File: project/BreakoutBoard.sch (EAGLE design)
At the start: 2 parts, among them J1 XF2L-2435-1, X1 LCD

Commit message: Layout complete
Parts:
- added B1: RESET, alps:SKSCLDE010
- added B2: BOOT, alps:SKSCLDE010
- added C1: 22pF/50V, SparkFun-Capacitors:22PF-0402T-16V-10%
- added C105: 2.2uF/16V, rcl:C-EUC0603
- added C106: 4.7uF/16V, rcl:C-EUC0603
- added C107: 22pF/50V, rcl:C-EUC0402
- added C17: 10uF/16V, rcl:C-EUC0603
- added C18: 0.1uF/10V, rcl:C-EUC0402
- added C19: 1uF/16V, rcl:C-EUC0402
- added C2, C5: 10uF/16V, SparkFun-Capacitors:10UF-0603-6.3V-20%
- added C3, C4: 0.1uF/10V, SparkFun-Capacitors:0.1UF-0402-10V-10%-X7R
- added C86: (no value), rcl:C-EUC0402
- added CN2: (no value), adafruit:JST_2PIN-SMT
- added D1, D15: (no value), diode:DIODE-SOD123
- added D10, D8, D9: LESD5D5.0CT1G, discrete:LESD5D5.0CT1G
- added D11, D12, D2: LESD8D3.3CAT5G, discrete:LESD8D3.3CAT5G
- added D19: (no value), adafruit:DIODESOD-523
- added D3: (no value), led:LEDCHIPLED_1206
- added J2: I2C2, SparkFun-Connectors:QWIIC_CONNECTOR
- added J3: LCD, ER-CON0.4-24P:ER-CON0.4-24
- added L1: 2.2μH, SparkFun-Coils:2.2μH-4X4-2.2μH-3A-45MOHM
- added L6: 10uH_0.8A, discrete:SRN3010TA
- added R1, R13: 10K, rcl:R-US_R0402
- added R111, R112: 0, rcl:R-US_R0201
- added R12, R123: 0, rcl:R-US_R0603
- added R126: 6.6, rcl:R-US_R0402
- added R127: 10, rcl:R-US_R0402
- added R2: 680K, rcl:R-US_R0402
- added R3: 150K, rcl:R-US_R0402
- added R74: 51, rcl:R-US_R0201
- added TP1, TP2: TEST-POINT3, SparkFun-Connectors:TEST-POINT3
- added U1: SY8088, discrete:SY8088
- added U15: BD60A60NUX, discrete:BD60A60NUX
- added U4: ESP32-S3-WROOM-1, espressif:ESP32-S3-WROOM-1
- J1: value XF2L-2435-1 -> I2C1; device con-omron:XF2L-2435-1 -> SparkFun-Connectors:QWIIC_CONNECTOR
- X1: value LCD -> (none); device ER-CON0.4-24P:ER-CON0.4-24 -> Adafruit ItsyBitsy nRF52840 Express:MICROBUILDER_USBMICRO_20329
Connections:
- removed net N$10: J1-10.MS, X1-10.1
- removed net N$11: J1-11.MS, X1-11.1
- removed net N$12: J1-12.MS, X1-12.1
- removed net N$13: J1-13.MS, X1-13.1
- removed net N$14: J1-14.MS, X1-14.1
- removed net N$15: J1-15.MS, X1-15.1
- removed net N$16: J1-16.MS, X1-16.1
- removed net N$17: J1-17.MS, X1-17.1
- removed net N$18: J1-18.MS, X1-18.1
- removed net N$19: J1-19.MS, X1-19.1
- removed net N$20: J1-20.MS, X1-20.1
- removed net N$21: J1-21.MS, X1-21.1
- removed net N$22: J1-22.MS, X1-22.1
- removed net N$23: J1-23.MS, X1-23.1
- removed net N$24: J1-24.MS, X1-24.1
- removed net N$3: J1-3.MS, X1-3.1
- removed net N$5: J1-5.MS, X1-5.1
- new net ESP_3V3: C17.1, C18.1, D2.C, R12.2, R13.1, U4.3V3
- new net GND: B1.1, B2.1, C105.2, C106.2, C107.2, C17.2, C18.2, C19.2, C2.2, C3.2, C4.2, C5.2, C86.2, CN2.1, D10.A, D11.A, D12.A, D2.A, D8.A, D9.A, J1.1, J2.1, J3-15.1, J3-16.1, J3-3.1, J3-4.1, R123.1, R126.1, R3.1, R74.1, TP2.1, U1.GND, U15.GND, U4.EPAD, U4.GND, U4.GND1
- new net GPIO0: B2.4, D12.C, U4.IO0
- new net GPIO18: J1.4, U4.IO18
- new net GPIO19: R111.2, U4.IO19
- new net GPIO20: R112.2, U4.IO20
- new net GPIO3: J3-21.1, U4.IO3
- new net GPIO4: J3-5.1, U4.IO4
- new net GPIO40: J2.4, J3-20.1, U4.IO40
- new net GPIO41: J2.3, J3-19.1, U4.IO41
- new net GPIO45: R127.1, U4.IO45
- new net GPIO48: J3-10.1, J3-18.1, U15.EN, U4.IO48
- new net GPIO5: J3-9.1, U4.IO5
- new net GPIO6: J3-8.1, U4.IO6
- new net GPIO7: J3-6.1, U4.IO7
- new net GPIO8: J1.3, U4.IO8
- new net LED_A: C105.1, D19.C, J3-23.1, J3-24.1, U15.VOUT
- new net LED_DIM: C107.1, R127.2, U15.PWM
- new net LED_K: J3-1.1, J3-2.1, U15.FB
- new net MCU_RST: B1.4, C19.1, D11.C, R13.2, U4.EN
- new net MCU_VDD: C1.1, C4.1, C5.1, C86.1, D3.A, J1.2, J2.2, J3-11.1, J3-12.1, J3-13.1, J3-14.1, J3-17.1, L1.2, R12.1, R2.2, TP1.1
- new net USB_5V: C106.1, C2.1, C3.1, D1.C, D15.C, L6.1, R1.1, U1.IN, U15.VIN
- new net USB_DN: D9.C, R111.1, X1.D-
- new net USB_DP: D10.C, R112.1, X1.D+
- new net USB_G: R123.2, X1.GND
- new net USB_VBUS: D1.A, D8.C, X1.VBUS
- net N$1: now also D19.A, L6.2, U15.SW; no longer J1-1.MSV, X1-1.1
- net N$2: now also D3.C, R74.2; no longer J1-2.MS, X1-2.1
- net N$4: now also CN2.2, D15.A; no longer J1-4.MS, X1-4.1
- net N$6: now also R1.2, U1.EN; no longer J1-6.MS, X1-6.1
- net N$7: now also L1.1, U1.LX; no longer J1-7.MS, X1-7.1
- net N$8: now also C1.2, R2.1, R3.2, U1.FB; no longer J1-8.MS, X1-8.1
- net N$9: now also R126.2, U15.ISET; no longer J1-9.MS, X1-9.1

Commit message: Layout optimization
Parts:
- removed C107: 22pF/50V, rcl:C-EUC0402
- removed CN2: (no value), adafruit:JST_2PIN-SMT
- removed R127: 10, rcl:R-US_R0402
- removed TP2: TEST-POINT3, SparkFun-Connectors:TEST-POINT3
- removed X1: (no value), Adafruit ItsyBitsy nRF52840 Express:MICROBUILDER_USBMICRO_20329
- added C97: 0.1uF/6.3V, rcl:C-USC0402
- added C98: 4.7uF/6.3V, rcl:C-USC0402
- added J4: I2C1, SparkFun-Connectors:QWIIC_CONNECTOR
- added J5: I2C2, SparkFun-Connectors:QWIIC_CONNECTOR
- added U$1, U$2, U$4, U$5: FIDUCIAL, adafruit:FIDUCIAL
- B1, B2: LCSC (none) -> C115362
- C1: device SparkFun-Capacitors:22PF-0402T-16V-10% -> rcl:C-USC0402; LCSC (none) -> C106203
- C105: device rcl:C-EUC0603 -> rcl:C-USC0603; LCSC (none) -> C106853
- C106: device rcl:C-EUC0603 -> rcl:C-USC0603; LCSC (none) -> C277476
- C17: device rcl:C-EUC0603 -> rcl:C-USC0603; LCSC (none) -> C86275
- C18: device rcl:C-EUC0402 -> rcl:C-USC0402; LCSC (none) -> C161163
- C19: device rcl:C-EUC0402 -> rcl:C-USC0402; LCSC (none) -> C77007
- C2: device SparkFun-Capacitors:10UF-0603-6.3V-20% -> rcl:C-USC0603; LCSC (none) -> C86275
- C3: device SparkFun-Capacitors:0.1UF-0402-10V-10%-X7R -> rcl:C-USC0603; LCSC (none) -> C161163
- C4: device SparkFun-Capacitors:0.1UF-0402-10V-10%-X7R -> rcl:C-USC0402; LCSC (none) -> C161163
- C5: device SparkFun-Capacitors:10UF-0603-6.3V-20% -> rcl:C-USC0402; LCSC (none) -> C86275
- C86: value (none) -> 0.1uF/6.3V; device rcl:C-EUC0402 -> rcl:C-USC0402; LCSC (none) -> C541406
- D1, D15: LCSC (none) -> C511872
- D10, D8, D9: LCSC (none) -> C383211
- D11, D12, D2: LCSC (none) -> C172409
- D19: LCSC (none) -> C253516
- D3: LCSC (none) -> C375534
- J1: value I2C1 -> (none); device SparkFun-Connectors:QWIIC_CONNECTOR -> Adafruit ItsyBitsy nRF52840 Express:MICROBUILDER_USBMICRO_20329; LCSC (none) -> C40946
- J2: value I2C2 -> (none); device SparkFun-Connectors:QWIIC_CONNECTOR -> adafruit:JST_2PIN-SMT; LCSC (none) -> C64658
- L1: LCSC (none) -> C370436
- L6: LCSC (none) -> C518881
- R1, R13: LCSC (none) -> C60490
- R111, R112: LCSC (none) -> C106227
- R12, R123: LCSC (none) -> C100044
- R126: value 6.6 -> 20K; LCSC (none) -> C326980
- R2: LCSC (none) -> C163456
- R3: LCSC (none) -> C93947
- R74: LCSC (none) -> C163499
- TP1: value TEST-POINT3 -> TPTP06R; device SparkFun-Connectors:TEST-POINT3 -> testpad:TPTP06R
- U1: LCSC (none) -> C79313
- U15: LCSC (none) -> C2678724
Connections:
- removed net LED_DIM: C107.1, R127.2, U15.PWM
- net GND: now also B1.2, B2.2, C97.2, C98.2, J4.1, J5.1; no longer C107.2, CN2.1, J1.1, TP2.1
- net GPIO0: now also B2.3
- net GPIO18: now also J4.4; no longer J1.4
- net GPIO40: now also J5.4; no longer J2.4
- net GPIO41: now also J5.3; no longer J2.3
- net GPIO45: now also U15.PWM; no longer R127.1
- net GPIO8: now also J4.3; no longer J1.3
- net LED_K: now also TP1.TP
- net MCU_RST: now also B1.3
- net MCU_VDD: now also C97.1, C98.1, J4.2, J5.2, U15.VIN; no longer J1.2, J2.2, TP1.1
- net N$4: now also J2.2; no longer CN2.2
- net USB_5V: no longer U15.VIN
- net USB_DN: now also J1.D-; no longer X1.D-
- net USB_DP: now also J1.D+; no longer X1.D+
- net USB_G: now also J1.GND; no longer X1.GND
- net USB_VBUS: now also J1.VBUS; no longer X1.VBUS
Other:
- moved on the sheet: B1, B2, C1, C105, C106, C17, C18, C19, C2, C3, C4, C5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

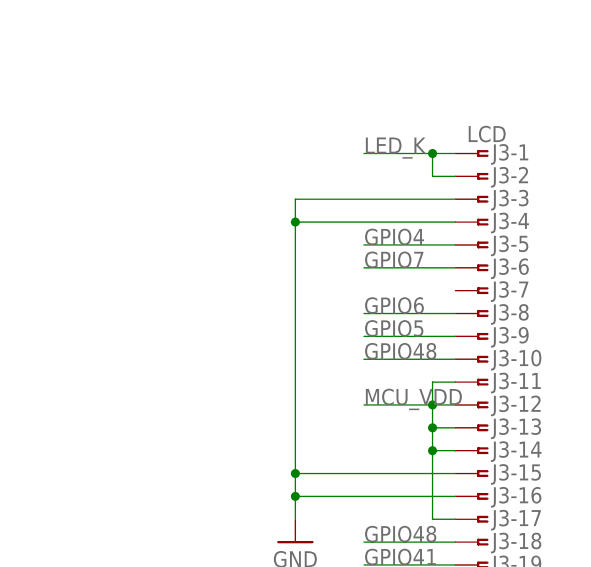
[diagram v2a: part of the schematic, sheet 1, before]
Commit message: Display pinout fix
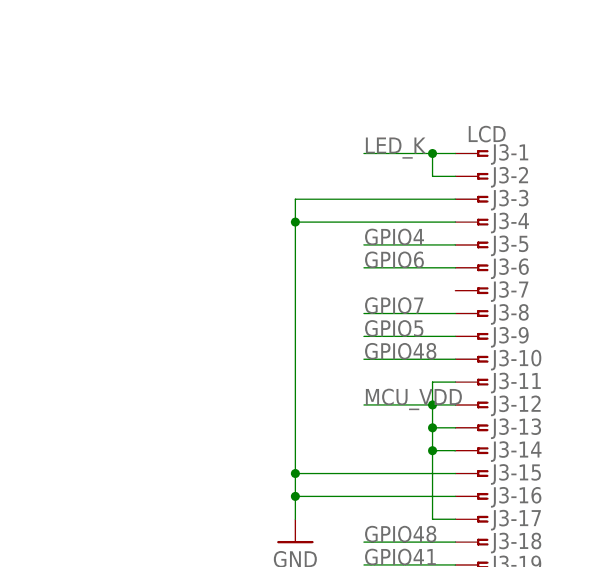
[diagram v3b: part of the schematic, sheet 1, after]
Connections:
- net GPIO6: now also J3-6.1; no longer J3-8.1
- net GPIO7: now also J3-8.1; no longer J3-6.1
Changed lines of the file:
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@@
 </segment>
 <segment>
-<pinref part="J3" gate="-8" pin="1"/>
-<wire x1="228.6" y1="83.82" x2="218.44" y2="83.82" width="0.1524" layer="91"/>
-<label x="218.44" y="83.82" size="1.778" layer="95"/>
+<pinref part="J3" gate="-6" pin="1"/>
+<wire x1="228.6" y1="88.9" x2="218.44" y2="88.9" width="0.1524" layer="91"/>
+<label x="218.44" y="88.9" size="1.778" layer="95"/>
 </segment>
 </net>
@@
 </segment>
 <segment>
-<pinref part="J3" gate="-6" pin="1"/>
-<wire x1="228.6" y1="88.9" x2="218.44" y2="88.9" width="0.1524" layer="91"/>
-<label x="218.44" y="88.9" size="1.778" layer="95"/>
+<pinref part="J3" gate="-8" pin="1"/>
+<wire x1="228.6" y1="83.82" x2="218.44" y2="83.82" width="0.1524" layer="91"/>
+<label x="218.44" y="83.82" size="1.778" layer="95"/>
 </segment>
 </net>
